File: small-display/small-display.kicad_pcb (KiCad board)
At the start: 4 copper layers, 43 x 62 mm, 46 parts, among them J1 2047110001, J2 Micro_SD_Card_Det, J5 F32D-1A7Y1-21040, U1 TPD4EUSB30, U2 74LVC1G07SE-7, U3 RT9742GGJ5, U4 PAM2804AAB010, U5 USB2412-DZK, U6 NLVVHC1G04DFT1G, U7 M24M01-DFDW6TP, Y1 ECS-240-8-33-AGN-TR

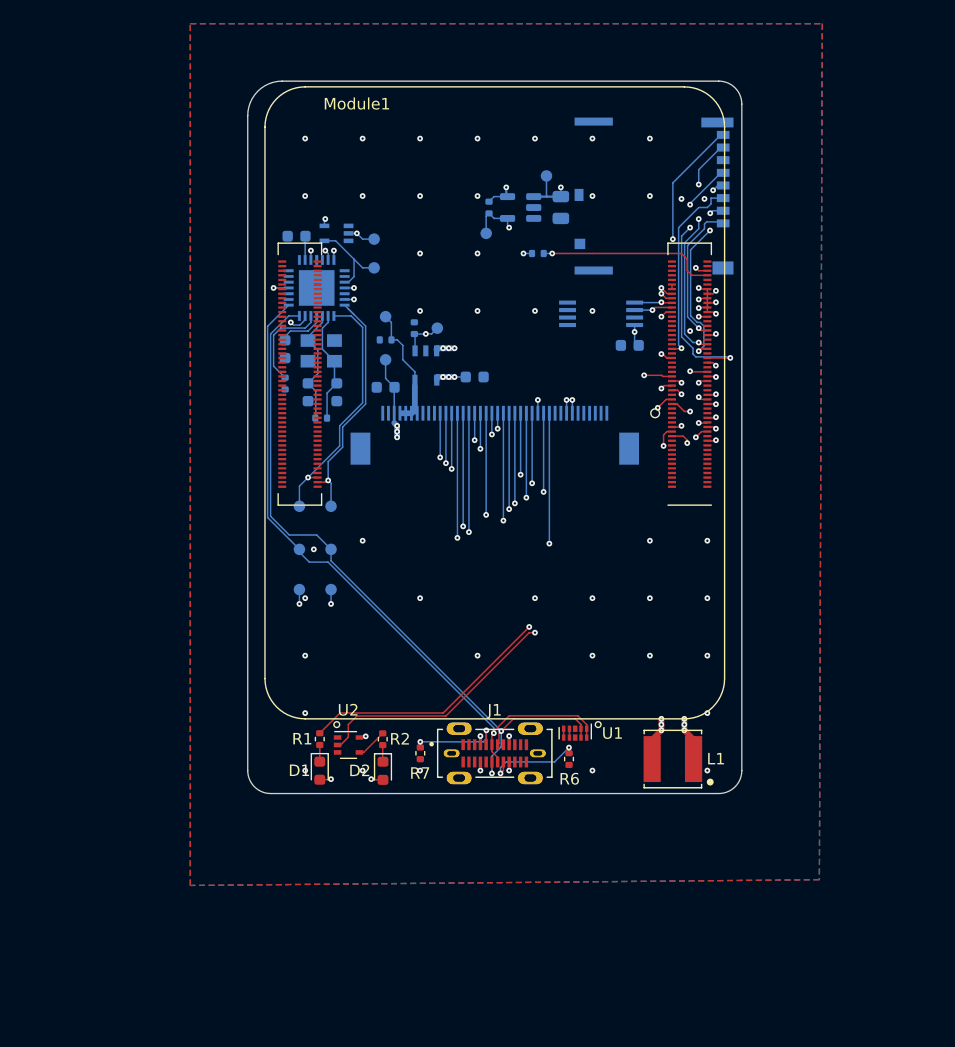
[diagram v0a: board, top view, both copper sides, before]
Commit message: Added 4.7k I2C pullup resistors.
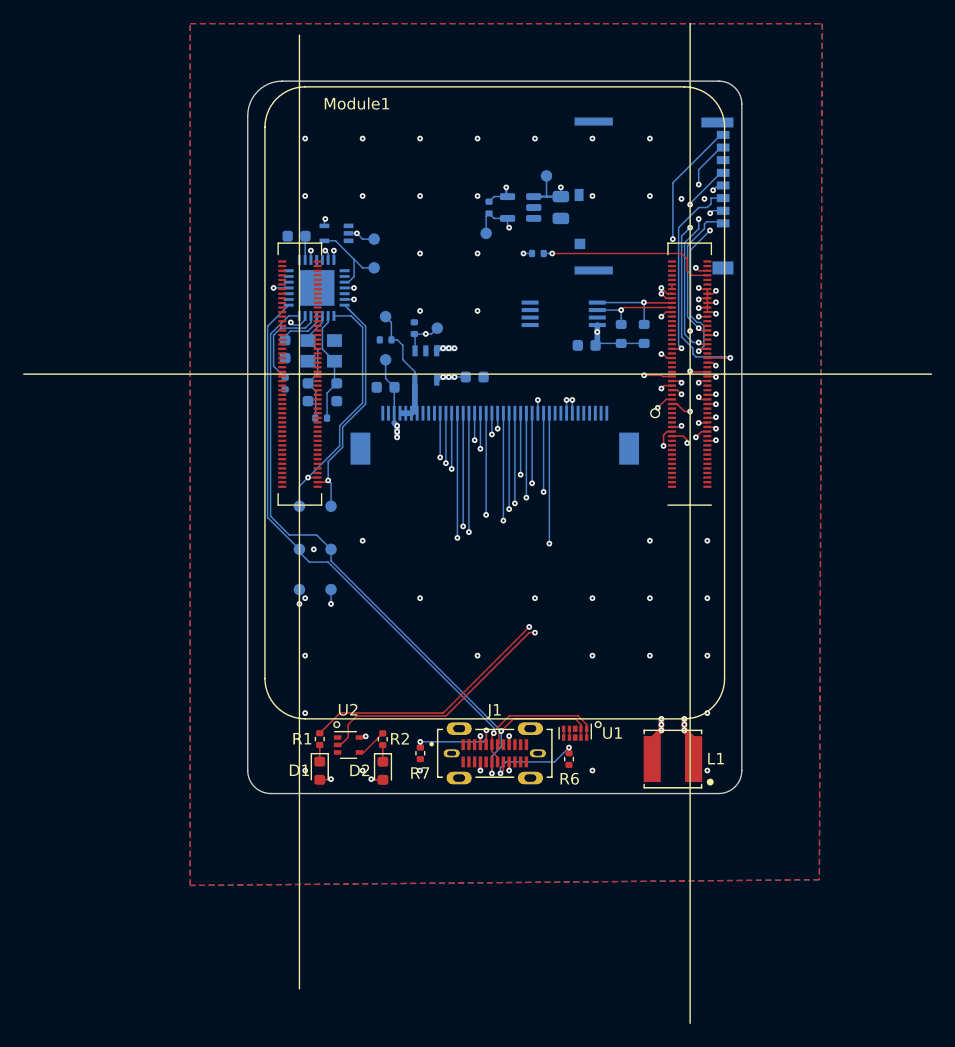
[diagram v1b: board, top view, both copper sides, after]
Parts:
- added R11: 4.7k, Resistor_SMD:R_0603_1608Metric, B.Cu at (34.5, 22.0)
- added R12: 4.7k, Resistor_SMD:R_0603_1608Metric, B.Cu at (32.5, 22.0)
- moved C6 3.75 mm to (29.5, 23.0)
- moved U7 3.25 mm to (27.5, 20.2)
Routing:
- net SDA0: track 3.28 -> 8.46 mm
- net SCL0: track 3.34 -> 7.84 mm
- net +3.3V: track 23.0 -> 27.2 mm
- net GND: vias 45 -> 43

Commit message: Added logo and copyright.
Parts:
- added G***: LOGO, airball-hardware:airball-logo-5mm, B.Cu at (21.0, 3.75)
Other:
- board text added: "Airball Small Display Copyright © 2023, The Airball authors 2023-12-08"
